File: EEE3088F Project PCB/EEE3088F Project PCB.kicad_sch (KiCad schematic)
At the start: 64 parts, among them IC1 74LVC1G04SE-7, J1 JST PH 2.00mm connector, J2 TYPE-C-31-M-12, J3 TYPE-C-31-M-12, SW1 SS12D07VG5 087, U1 DRV8833PWR, U10 LM7805L-TF3-T, U11 TC4056A., U2 DRV8833PWPR, U3 INA219AxD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

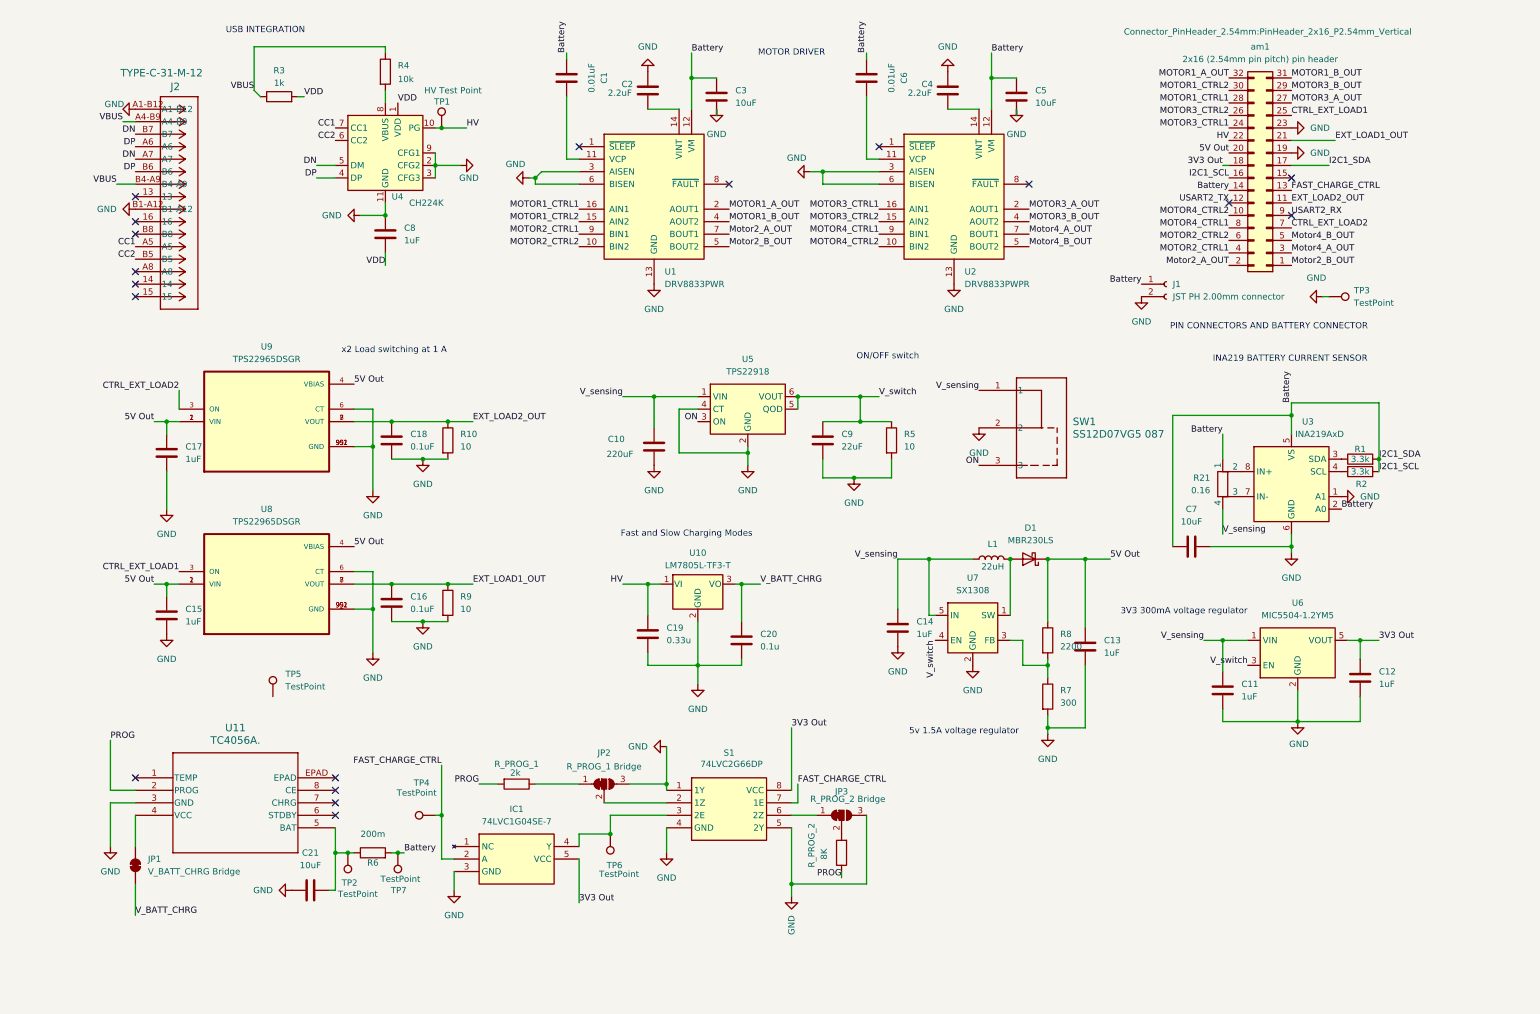
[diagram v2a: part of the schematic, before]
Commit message: ajusted some testing points and added footprints for USB integration + half of the charging requirments
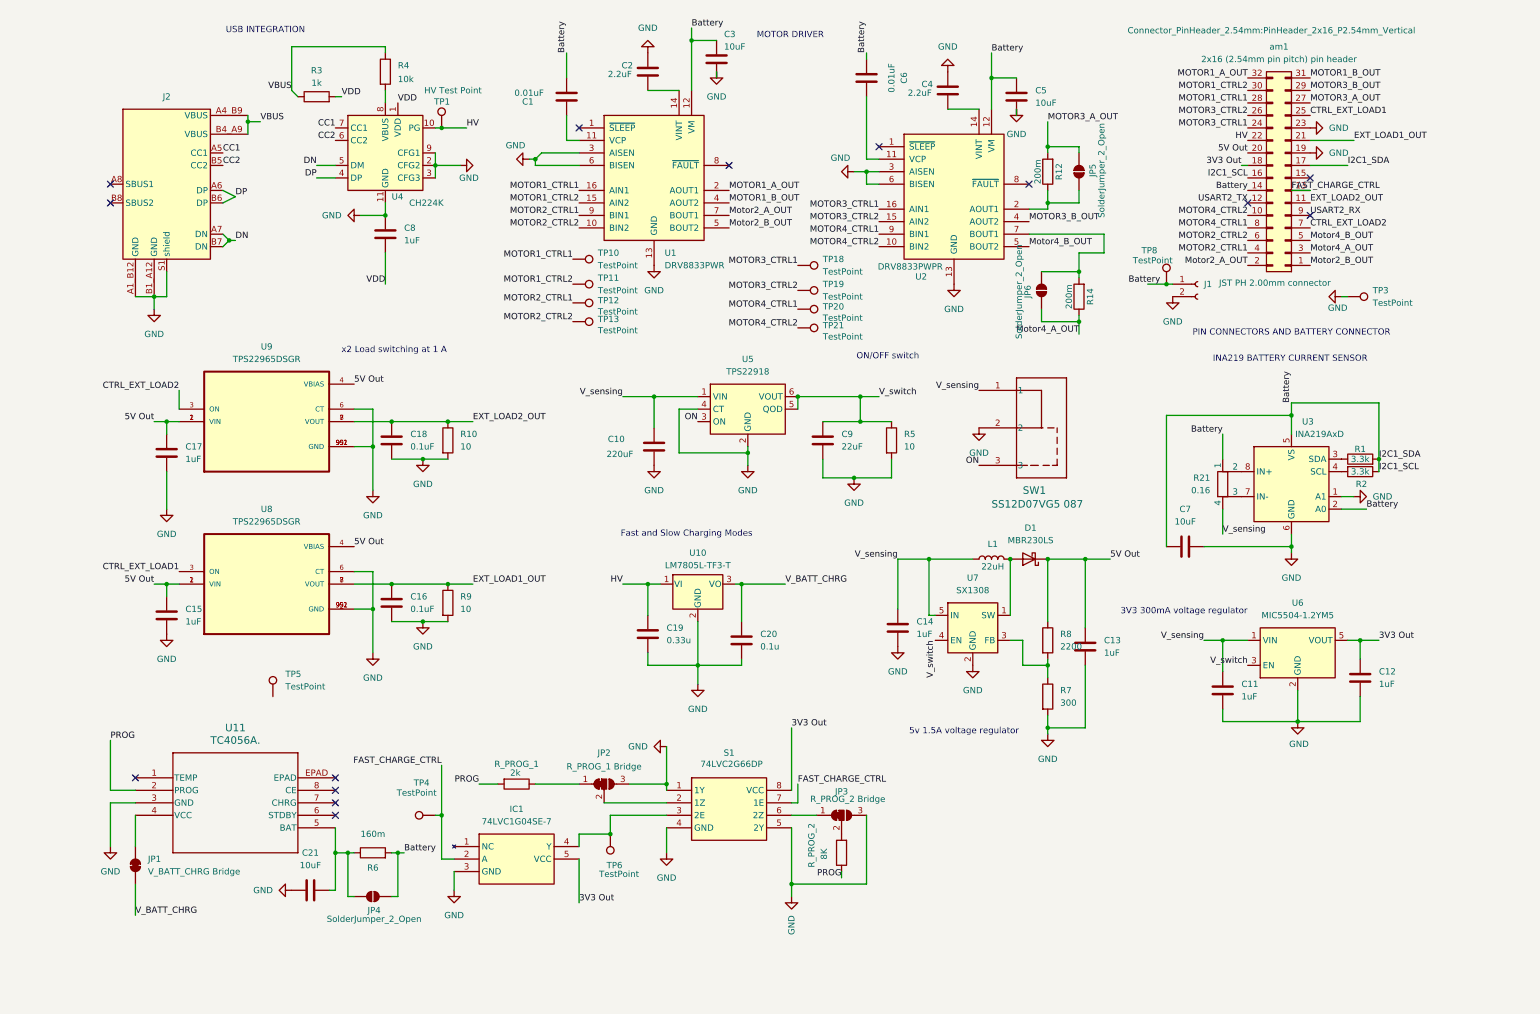
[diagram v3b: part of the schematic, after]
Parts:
- removed J2: TYPE-C-31-M-12, CONN12_C-31-M-12_HRO, symbol TYPE-C:TYPE-C-31-M-12
- removed TP2, TP7: TestPoint, TestPoint:TestPoint_Pad_1.0x1.0mm, symbol Connector:TestPoint
- added J2: ~, exported_footprints:HRO_TYPE-C-31-M-12, symbol Custom_symbols:TYPE-C-31-M-12
- added JP4, JP5, JP6: SolderJumper_2_Open, Jumper:SolderJumper-2_P1.3mm_Open_RoundedPad1.0x1.5mm, symbol Jumper:SolderJumper_2_Open
- added R12, R14: 200m, Resistor_SMD:R_Shunt_Vishay_WSR2_WSR3, symbol Device:R
- added TP10, TP11, TP12, TP13, TP18, TP19, TP20, TP21, TP8: TestPoint, symbol Connector:TestPoint
- R6: value 200m -> 160m; footprint Resistor_SMD:R_Shunt_Vishay_WSR2_WSR3 -> Resistor_SMD:R_2512_6332Metric_Pad1.40x3.35mm_HandSolder
- U10: footprint Package_TO_SOT_THT:TO-220-3_Vertical -> Package_TO_SOT_THT:TO-220F-3_Vertical
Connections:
- net Battery: now also JP4.1 (A), TP8.1
- net CC1: now also J2.A5 (CC1)
- net CC2: now also J2.B5 (CC2)
- net DN: now also J2.A7 (DN), J2.B7 (DN)
- net DP: now also J2.A6 (DP), J2.B6 (DP)
- net GND: now also J2.A1_B12 (GND), J2.B1_A12 (GND), J2.S1 (shield)
- net MOTOR1_CTRL1: now also TP10.1
- net MOTOR1_CTRL2: now also TP11.1
- net MOTOR2_CTRL1: now also TP12.1
- net MOTOR2_CTRL2: now also TP13.1
- net MOTOR3_A_OUT: now also JP5.1 (A), R12.2; no longer U2.2 (AOUT1)
- net MOTOR3_CTRL1: now also TP18.1
- net MOTOR3_CTRL2: now also TP19.1
- net MOTOR4_CTRL1: now also TP20.1
- net MOTOR4_CTRL2: now also TP21.1
- net Motor4_A_OUT: now also JP6.1 (A), R14.1; no longer U2.7 (BOUT1)
- net VBUS: now also J2.A4_B9 (VBUS), J2.B4_A9 (VBUS)
- net at C21.2, R6.1, U11.5 (BAT): now also JP4.2 (B)
- new net: JP5.2 (B), R12.1, U2.2 (AOUT1)
- new net: JP6.2 (B), R14.2, U2.7 (BOUT1)
- no-connect marks 18 -> 14
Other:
- moved on the sheet: C1, C2, C3, C7, J1, R3, TP3, U1, am1

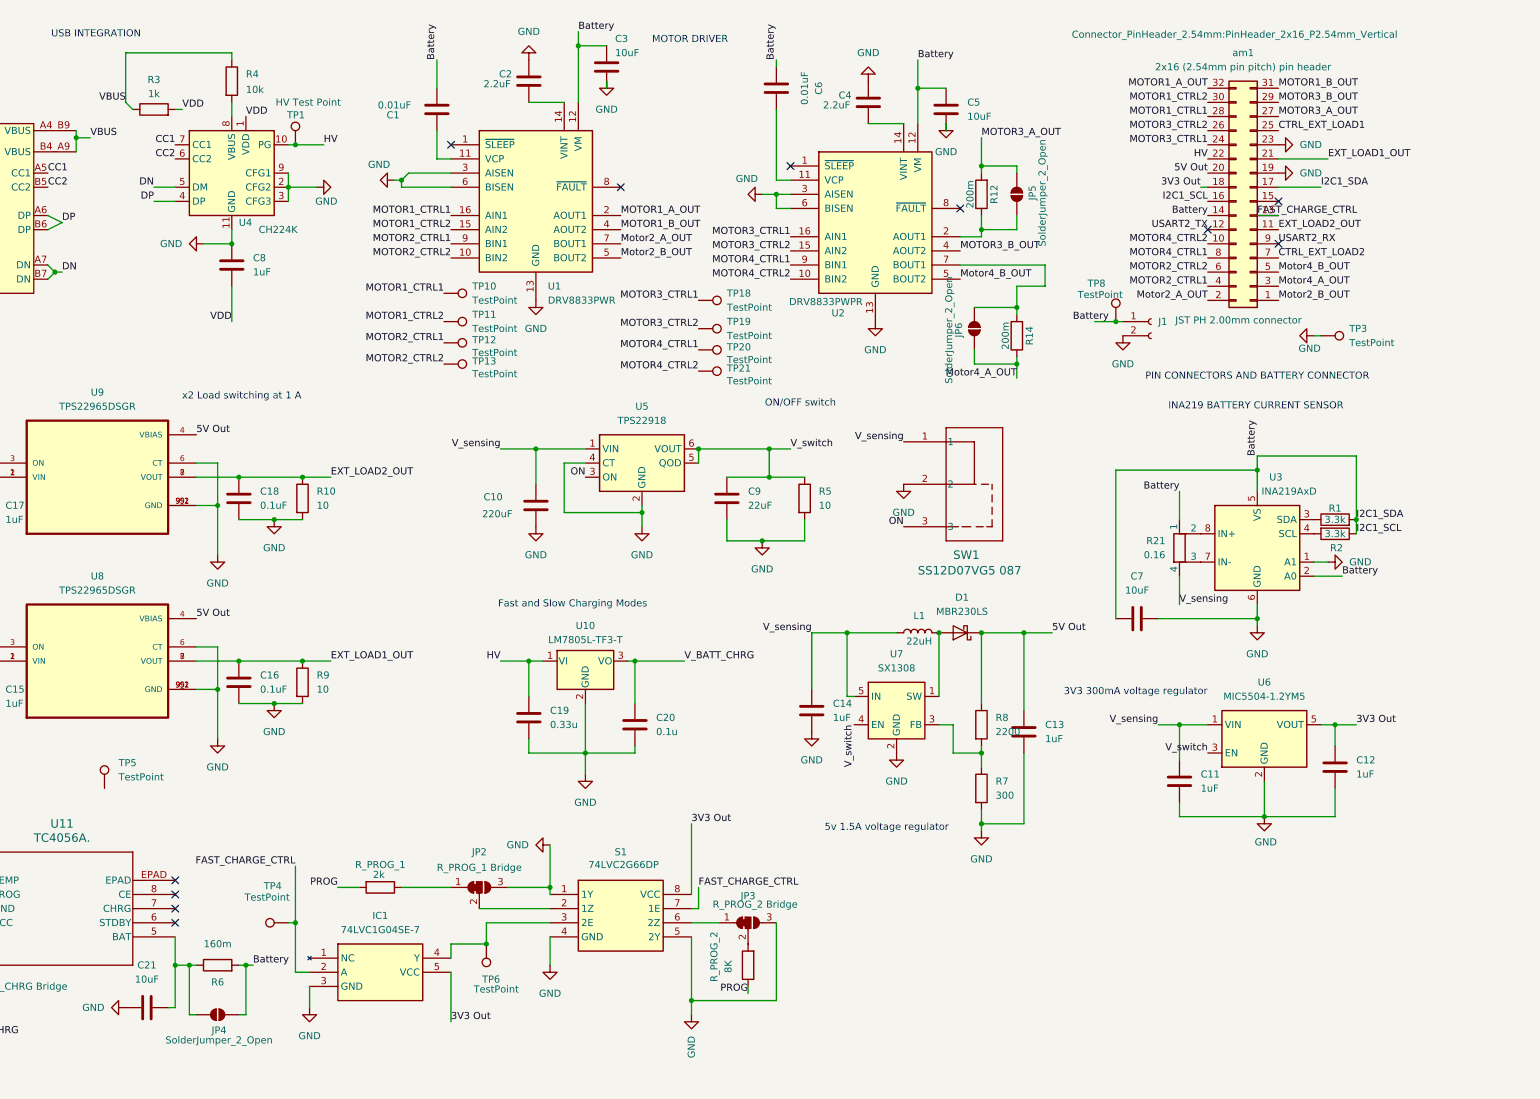
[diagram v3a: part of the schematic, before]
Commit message: added footprints to all my componets, placed all components on the board, and added all my jlcpcb part numbers
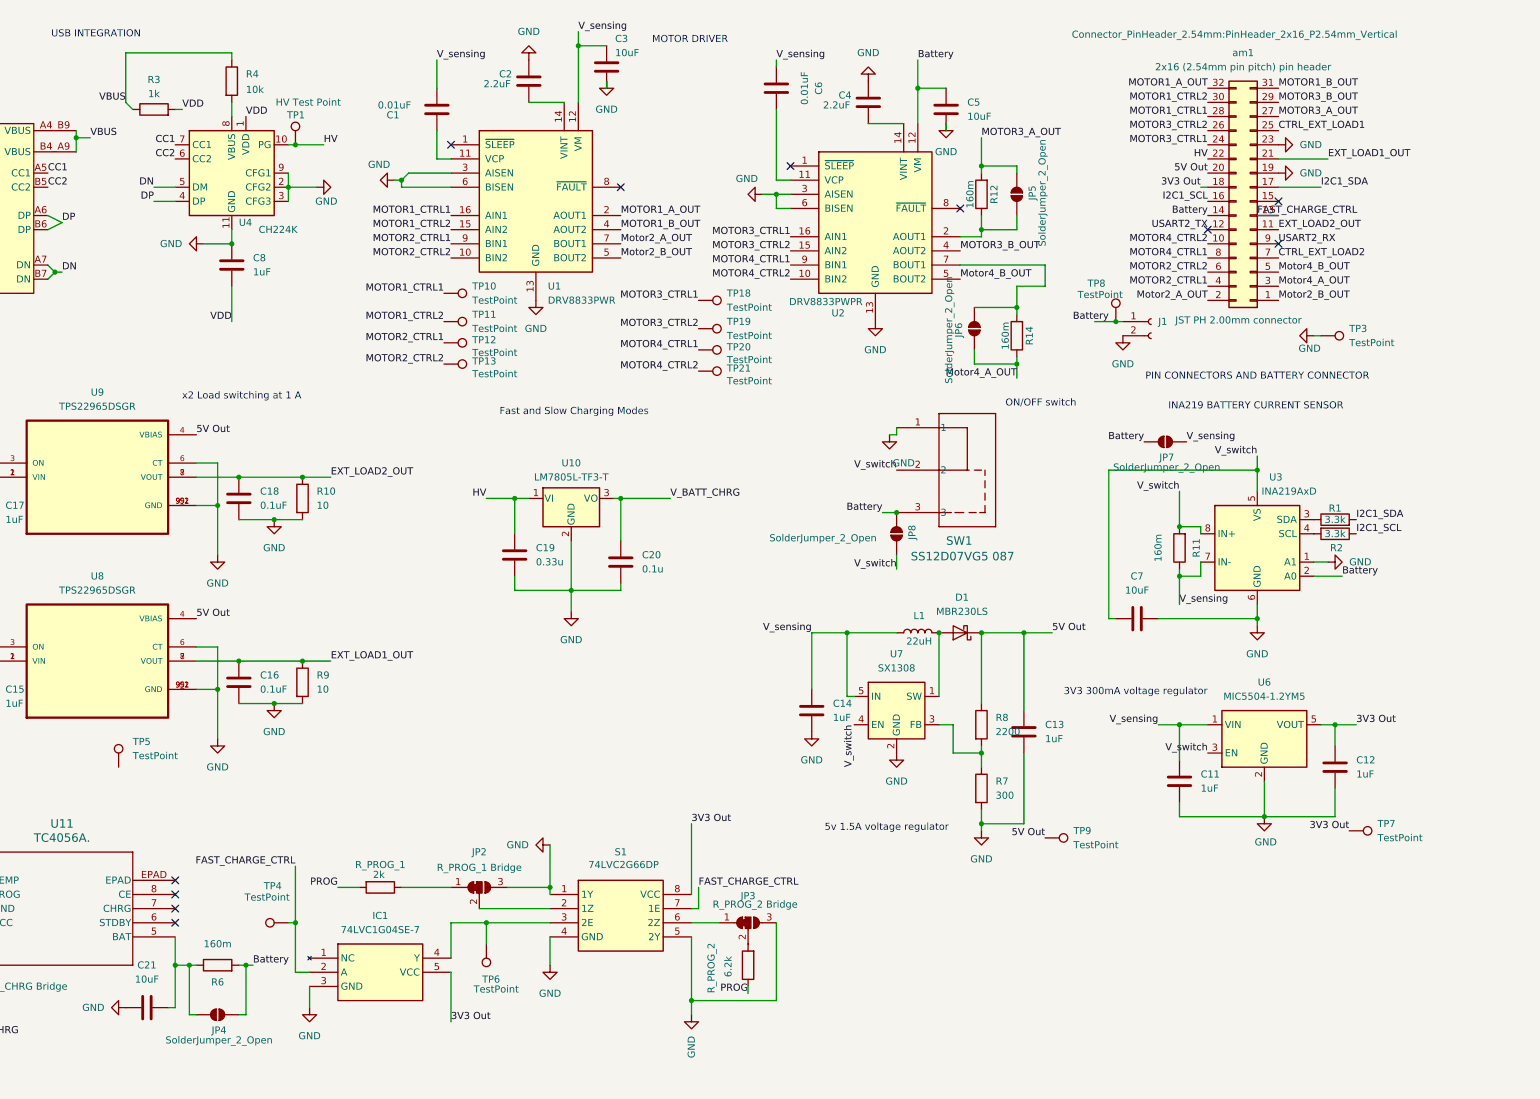
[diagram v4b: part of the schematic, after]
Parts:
- removed C10: 220uF, exported_footprints:CAPC2012X140N, symbol Device:C
- removed C9: 22uF, exported_footprints:CAPC2012X140N, symbol Device:C
- removed R21: 0.16, exported_footprints:CAPC3216X180N, symbol Device:R_Shunt
- removed R5: 10, exported_footprints:RESC3115X65N, symbol Device:R
- removed U5: TPS22918, Package_TO_SOT_SMD:SOT-23-6, symbol Power_Management:TPS22917DBV
- added JP7, JP8: SolderJumper_2_Open, Jumper:SolderJumper-2_P1.3mm_Open_RoundedPad1.0x1.5mm, symbol Jumper:SolderJumper_2_Open
- added R11: 160m, Resistor_SMD:R_2512_6332Metric_Pad1.40x3.35mm_HandSolder, symbol Device:R
- added TP7, TP9: TestPoint, TestPoint:TestPoint_Pad_2.0x2.0mm, symbol Connector:TestPoint
- C1, C19, C6: footprint exported_footprints:CAPC2012X140N -> Capacitor_SMD:C_0805_2012Metric_Pad1.18x1.45mm_HandSolder
- C11, C12, C13, C14, C15, C17: footprint exported_footprints:CAPC3216X180N -> Capacitor_SMD:C_1206_3216Metric_Pad1.33x1.80mm_HandSolder
- C16, C18: footprint exported_footprints:CAPC2012X140N -> Capacitor_SMD:C_0402_1005Metric_Pad0.74x0.62mm_HandSolder
- C2, C4: footprint exported_footprints:CAPC1608X90N -> Capacitor_SMD:C_0603_1608Metric_Pad1.08x0.95mm_HandSolder
- C20: footprint exported_footprints:RESC3115X65N -> Capacitor_SMD:C_0402_1005Metric_Pad0.74x0.62mm_HandSolder
- C21, C3, C5: footprint exported_footprints:CAPC1005X55N -> Capacitor_SMD:C_0805_2012Metric_Pad1.18x1.45mm_HandSolder
- C7: footprint exported_footprints:CAPC1005X55N -> Capacitor_SMD:C_0402_1005Metric_Pad0.74x0.62mm_HandSolder
- IC1: footprint exported_footprints:74LVC1G04SE-7 -> Package_TO_SOT_SMD:SOT-353_SC-70-5_Handsoldering
- JP2: footprint (none) -> Jumper:SolderJumper-3_P1.3mm_Bridged2Bar12_RoundedPad1.0x1.5mm_NumberLabels
- JP3: footprint Jumper:SolderJumper-3_P1.3mm_Bridged2Bar12_Pad1.0x1.5mm_NumberLabels -> Jumper:SolderJumper-3_P1.3mm_Bridged2Bar12_RoundedPad1.0x1.5mm_NumberLabels
- L1: footprint exported_footprints:SMNR5040-220MT -> Inductor_SMD:L_Ferrocore_DLG-0403
- R1, R2: footprint exported_footprints:RESC3115X65N -> Resistor_SMD:R_0603_1608Metric
- R10, R9: footprint exported_footprints:RESC3115X65N -> Resistor_SMD:R_1206_3216Metric_Pad1.30x1.75mm_HandSolder
- R12, R14: value 200m -> 160m; footprint Resistor_SMD:R_Shunt_Vishay_WSR2_WSR3 -> Resistor_SMD:R_2512_6332Metric_Pad1.40x3.35mm_HandSolder
- R7: footprint exported_footprints:RESC3115X65N -> Resistor_SMD:R_0805_2012Metric_Pad1.20x1.40mm_HandSolder
- R8: footprint exported_footprints:RESC3115X65N -> Resistor_SMD:R_0603_1608Metric_Pad0.98x0.95mm_HandSolder
- R_PROG_1: footprint exported_footprints:RESC3115X65N -> Resistor_SMD:R_0402_1005Metric_Pad0.72x0.64mm_HandSolder
- R_PROG_2: value 8K -> 6.2k; footprint exported_footprints:RESC3115X65N -> Resistor_SMD:R_0603_1608Metric
- TP6: footprint (none) -> TestPoint:TestPoint_Pad_1.0x1.0mm
- U1, U2: footprint exported_footprints:SOP65P640X120-16N -> Package_SO:TSSOP-16-1EP_4.4x5mm_P0.65mm_EP3x3mm
- U3: footprint Package_SO:SOIC-8_3.9x4.9mm_P1.27mm -> Package_TO_SOT_SMD:TSOT-23-8
- U8, U9: footprint exported_footprints:SON50P200X200X80-9N -> Package_DFN_QFN:DFN-8-1EP_2x2mm_P0.5mm_EP0.9x1.6mm
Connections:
- net ON is gone; now on net Battery: SW1.3
- net 3V3 Out: now also TP7.1
- net 5V Out: now also TP9.1
- net Battery: now also JP7.2 (B), JP8.1 (A); no longer C1.1, C3.2, C6.1, C7.1, R1.2, R2.1, U1.12 (VM), U3.5 (VS), am1.16 (Pin_16), am1.17 (Pin_17)
- net GND: now also SW1.1; no longer SW1.2
- net V_sensing: now also C1.1, C3.2, C6.1, U1.12 (VM), U3.7 (IN-), JP7.1 (A), R11.1; no longer SW1.1
- net V_switch: now also C7.1, SW1.2, U3.5 (VS), U3.8 (IN+), JP8.2 (B), R11.2
- new net I2C1_SCL: R2.1, am1.16 (Pin_16)
- new net I2C1_SDA: R1.2, am1.17 (Pin_17)
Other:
- moved on the sheet: C19, C20, SW1, TP5, U10

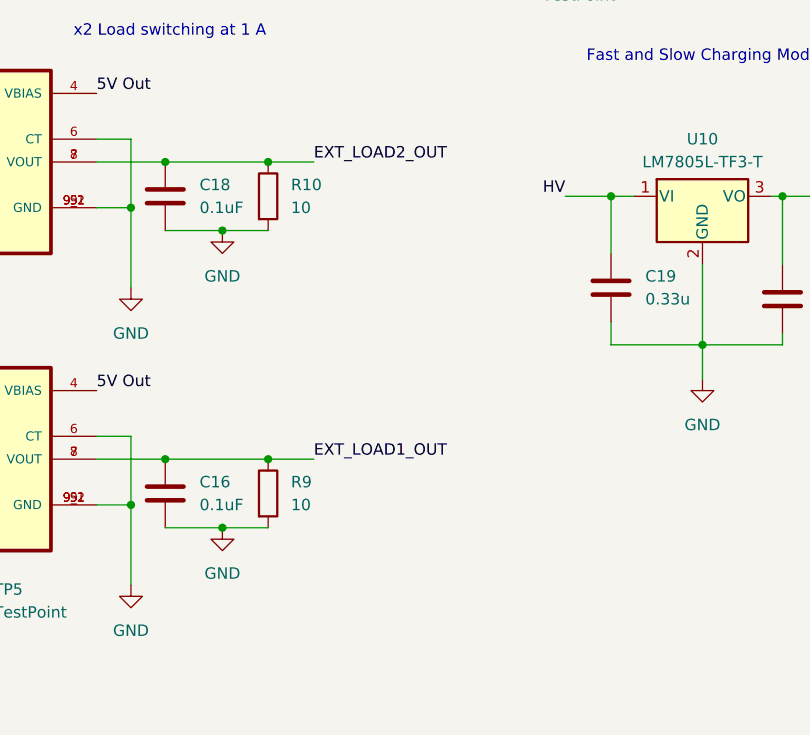
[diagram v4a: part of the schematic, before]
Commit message: confimed all tadala footprints, as well as placed all footprints on PCB board
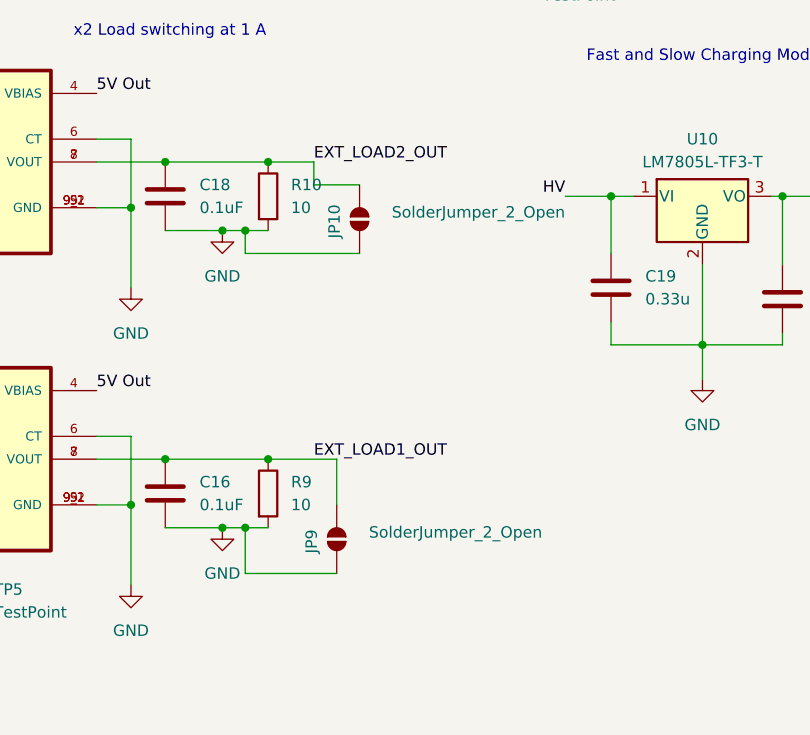
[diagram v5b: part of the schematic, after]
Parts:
- added JP10, JP9: SolderJumper_2_Open, Jumper:SolderJumper-2_P1.3mm_Open_RoundedPad1.0x1.5mm, symbol Jumper:SolderJumper_2_Open
- C11, C12, C13, C14, C15, C17: footprint Capacitor_SMD:C_1206_3216Metric_Pad1.33x1.80mm_HandSolder -> Capacitor_SMD:C_0805_2012Metric_Pad1.18x1.45mm_HandSolder
- C7: footprint Capacitor_SMD:C_0402_1005Metric_Pad0.74x0.62mm_HandSolder -> Capacitor_SMD:C_0805_2012Metric_Pad1.18x1.45mm_HandSolder
- L1: footprint Inductor_SMD:L_Ferrocore_DLG-0403 -> Inductor_SMD:L_Coilcraft_1515SQ-47N
- R7: footprint Resistor_SMD:R_0805_2012Metric_Pad1.20x1.40mm_HandSolder -> Resistor_SMD:R_0402_1005Metric_Pad0.72x0.64mm_HandSolder
- R8: footprint Resistor_SMD:R_0603_1608Metric_Pad0.98x0.95mm_HandSolder -> Resistor_SMD:R_0402_1005Metric_Pad0.72x0.64mm_HandSolder
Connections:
- net EXT_LOAD1_OUT: now also JP9.2 (B)
- net EXT_LOAD2_OUT: now also JP10.2 (B)
- net GND: now also JP10.1 (A), JP9.1 (A)
